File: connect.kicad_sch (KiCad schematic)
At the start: 37 parts, among them J101 Cortex, J102 DX07S016JA3, SW101 SKSG, SW102 SKSG, SW103 SKSG, SW104 SKSG, SW105 SKSG, U101 TPS78433QWDRBRQ1, U102 ATSAMD51J, Y101 32k768

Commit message: Refresh
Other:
- moved on the sheet: D102, D103, ESD101

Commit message: Export stencil
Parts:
- C107, C110: Manufacturer YAGEO -> TDK; Mouser 603-CC603JRNPO9BN180 -> 810-CGA3E2C0G1H180J; Product CC0603JRNPO9BN180 -> CGA3E2C0G1H180J080AA
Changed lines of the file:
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@@
 	(title_block
 		(title "V2 connect")
-		(date "2026-02-12")
+		(date "2026-03-02")
 		(rev "2026-02-12")
 		(company "Versio Duo")
@@
 			)
 		)
-		(property "Mouser" "603-CC603JRNPO9BN180"
+		(property "Mouser" "810-CGA3E2C0G1H180J"
 			(at 0.762 43.18 0)
 			(show_name yes)
@@
 			)
 		)
-		(property "Product" "CC0603JRNPO9BN180"
+		(property "Product" "CGA3E2C0G1H180J080AA"
 			(at 3.556 43.18 0)
 			(show_name yes)
@@
 			)
 		)
-		(property "Manufacturer" "YAGEO"
+		(property "Manufacturer" "TDK"
 			(at 6.35 43.18 0)
 			(show_name yes)
@@
 			)
 		)
-		(property "Mouser" "603-CC603JRNPO9BN180"
+		(property "Mouser" "810-CGA3E2C0G1H180J"
 			(at 0.762 38.1 0)
 			(show_name yes)
@@
 			)
 		)
-		(property "Product" "CC0603JRNPO9BN180"
+		(property "Product" "CGA3E2C0G1H180J080AA"
 			(at 3.556 38.1 0)
 			(show_name yes)
@@
 			)
 		)
-		(property "Manufacturer" "YAGEO"
+		(property "Manufacturer" "TDK"
 			(at 6.35 38.1 0)
 			(show_name yes)

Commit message: Replace diode
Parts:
- D102, D103, D104: Rating (none) -> 60V
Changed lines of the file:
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@@
 	(title_block
 		(title "V2 connect")
-		(date "2026-03-02")
-		(rev "2026-02-12")
+		(date "2026-03-12")
+		(rev "2026-03-12")
 		(company "Versio Duo")
 	)
@@
 			)
 		)
-		(property "Description" "Unpolarized capacitor, small symbol"
+		(property "Description" ""
 			(at 57.15 171.45 0)
 			(effects
@@
 			)
 		)
-		(property "Description" "Push button switch, generic, two pins"
+		(property "Description" "Push button"
 			(at 264.16 24.13 0)
 			(effects
@@
 			)
 		)
-		(property "Description" "Unpolarized capacitor, small symbol"
+		(property "Description" ""
 			(at 88.9 39.37 0)
 			(effects
@@
 			)
 		)
-		(property "Description" "Two pin crystal, small symbol"
+		(property "Description" ""
 			(at 26.67 40.64 0)
 			(effects
@@
 			)
 		)
-		(property "Description" "Light emitting diode, small symbol"
+		(property "Description" ""
 			(at 132.08 58.42 0)
 			(effects
@@
 			)
 		)
-		(property "Description" "Unpolarized capacitor, small symbol"
+		(property "Description" ""
 			(at 198.12 54.61 0)
 			(effects
@@
 			)
 		)
-		(property "Description" "Unpolarized capacitor, small symbol"
+		(property "Description" ""
 			(at 9.652 43.18 0)
 			(effects
@@
 			)
 		)
-		(property "Description" "Resistor, small symbol"
+		(property "Description" ""
 			(at 219.71 88.9 0)
 			(effects
@@
 			)
 		)
-		(property "Description" "Push button switch, generic, two pins"
+		(property "Description" "Push button"
 			(at 264.16 58.42 0)
 			(effects
@@
 			)
 		)
+		(property "Rating" "60V"
+			(at 71.12 137.16 0)
+			(effects
+				(font
+					(size 1.27 1.27)
+				)
+				(hide yes)
+			)
+		)
 		(pin "1"
 		)
@@
 			)
 		)
-		(property "Description" "Unpolarized capacitor, small symbol"
+		(property "Description" ""
 			(at 173.99 54.61 0)
 			(effects
@@
 			)
 		)
-		(property "Description" "Unpolarized capacitor, small symbol"
+		(property "Description" ""
 			(at 119.38 39.37 0)
 			(effects
@@
 			)
 		)
-		(property "Description" "Resistor, small symbol"
+		(property "Description" ""
 			(at 219.71 91.44 0)
 			(effects
@@
 			)
 		)
+		(property "Rating" "60V"
+			(at 257.81 107.95 0)
+			(effects
+				(font
+					(size 1.27 1.27)
+				)
+				(hide yes)
+			)
+		)
 		(pin "1"
 		)
@@
 			)
 		)
-		(property "Description" "Resistor, small symbol"
+		(property "Description" ""
 			(at 63.5 120.65 0)
 			(effects
@@
 			)
 		)
-		(property "Description" "Unpolarized capacitor, small symbol"
+		(property "Description" ""
 			(at 9.652 38.1 0)
 			(effects
@@
 			)
 		)
-		(property "Description" "Resistor, small symbol"
+		(property "Description" ""
 			(at 152.4 58.42 0)
 			(effects
@@
 			)
 		)
-		(property "Description" "Unpolarized capacitor, small symbol"
+		(property "Description" ""
 			(at 99.06 39.37 0)
 			(effects
@@
 			)
 		)
-		(property "Description" "Unpolarized capacitor, small symbol"
+		(property "Description" ""
 			(at 78.74 39.37 0)
 			(effects
@@
 			)
 		)
-		(property "Description" "Push button switch, generic, two pins"
+		(property "Description" "Push button"
 			(at 133.35 76.2 0)
 			(effects
@@
 			)
 		)
-		(property "Description" "Unpolarized capacitor, small symbol"
+		(property "Description" ""
 			(at 109.22 39.37 0)
 			(effects
@@
 			)
 		)
+		(property "Rating" "60V"
+			(at 257.81 92.71 0)
+			(effects
+				(font
+					(size 1.27 1.27)
+				)
+				(hide yes)
+			)
+		)
 		(pin "1"
 		)
@@
 			)
 		)
-		(property "Description" "Push button switch, generic, two pins"
+		(property "Description" "Push button"
 			(at 264.16 46.99 0)
 			(effects
@@
 			)
 		)
-		(property "Description" "Unpolarized capacitor, small symbol"
+		(property "Description" ""
 			(at 57.15 41.91 0)
 			(effects
@@
 			)
 		)
-		(property "Description" "Push button switch, generic, two pins"
+		(property "Description" "Push button"
 			(at 264.16 35.56 0)
 			(effects

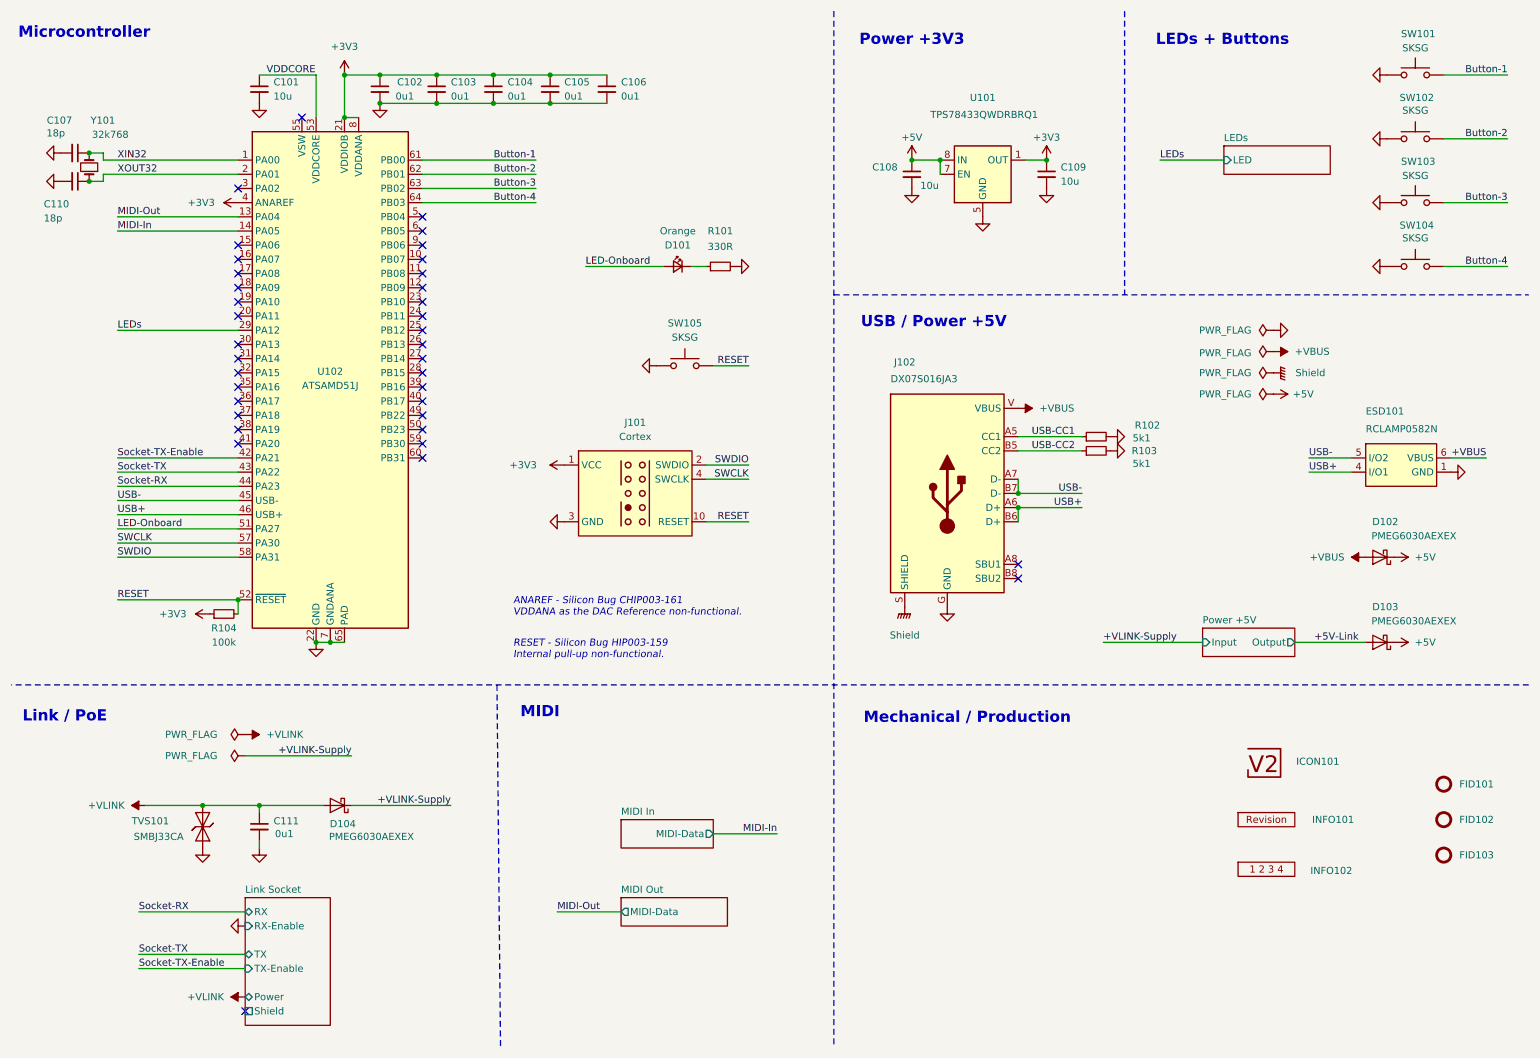
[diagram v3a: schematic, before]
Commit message: Update ESD suppressor
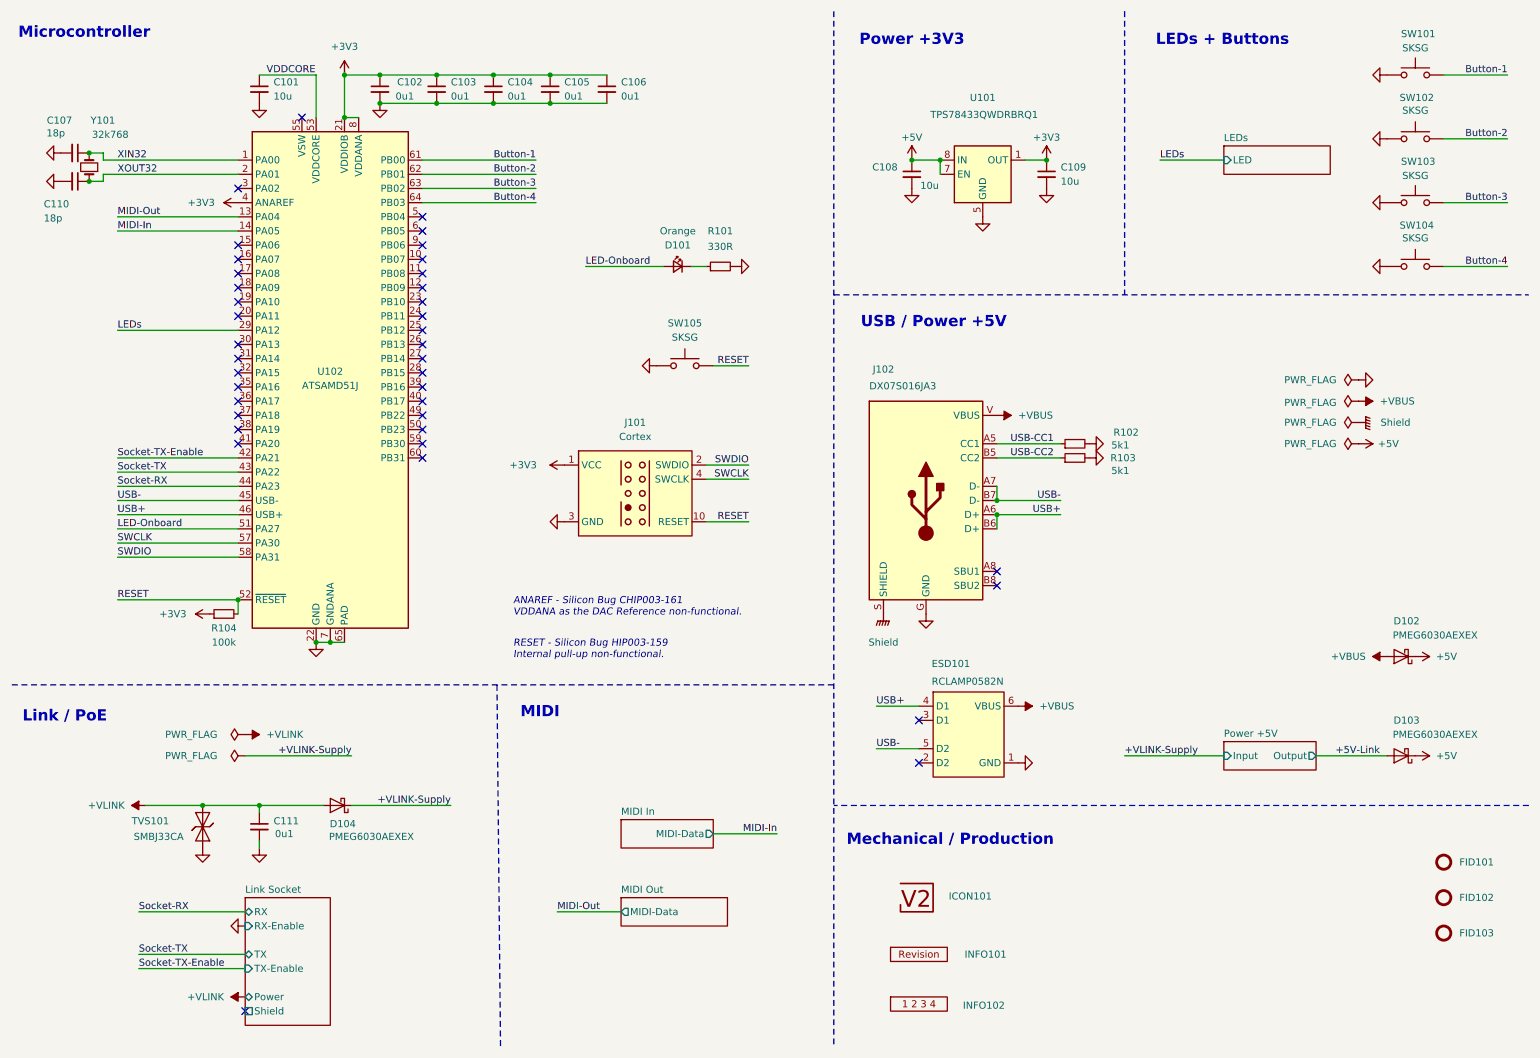
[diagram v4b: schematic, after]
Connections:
- no-connect marks 37 -> 39
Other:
- moved on the sheet: D102, D103, FID101, FID102, FID103, ICON101, INFO101, INFO102, J102, R102, R103

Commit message: Update
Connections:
- net USB+: now also ESD101.3 (D1)
- net USB-: now also ESD101.2 (D2)
- no-connect marks 39 -> 37
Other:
- moved on the sheet: D102, D103
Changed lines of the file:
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@@
 	)
 	(junction
+		(at 175.26 137.16)
+		(diameter 0)
+		(color 0 0 0 0)
+	)
+	(junction
 		(at 46.99 154.94)
 		(diameter 0)
@@
 	)
 	(junction
+		(at 175.26 144.78)
+		(diameter 0)
+		(color 0 0 0 0)
+	)
+	(junction
 		(at 78.74 29.21)
 		(diameter 0)
@@
 	)
 	(no_connect
-		(at 175.26 147.32)
-	)
-	(no_connect
 		(at 64.77 31.75)
 	)
@@
 	)
 	(no_connect
-		(at 175.26 139.7)
-	)
-	(no_connect
 		(at 86.36 72.39)
 	)
@@
 	(wire
 		(pts
-			(xy 246.38 146.05) (xy 259.08 146.05)
+			(xy 247.65 137.16) (xy 260.35 137.16)
 		)
 		(stroke
@@
 	(wire
 		(pts
-			(xy 229.87 146.05) (xy 212.09 146.05)
+			(xy 231.14 137.16) (xy 213.36 137.16)
 		)
 		(stroke
@@
 	(wire
 		(pts
+			(xy 175.26 137.16) (xy 175.26 139.7)
+		)
+		(stroke
+			(width 0)
+			(type default)
+		)
+	)
+	(wire
+		(pts
 			(xy 26.67 43.18) (xy 29.21 43.18)
 		)
@@
 	(wire
 		(pts
+			(xy 175.26 144.78) (xy 175.26 147.32)
+		)
+		(stroke
+			(width 0)
+			(type default)
+		)
+	)
+	(wire
+		(pts
 			(xy 137.16 96.52) (xy 144.78 96.52)
 		)
@@
 	)
 	(label "+5V-Link"
-		(at 257.81 146.05 180)
+		(at 259.08 137.16 180)
 		(effects
 			(font
@@
 	)
 	(label "+VLINK-Supply"
-		(at 212.09 146.05 0)
+		(at 213.36 137.16 0)
 		(effects
 			(font
@@
 	(symbol
 		(lib_id "V2_power:+5V")
-		(at 264.16 146.05 270)
+		(at 265.43 137.16 270)
 		(unit 1)
 		(exclude_from_sim no)
@@
 		(dnp no)
 		(property "Reference" "#PWR130"
-			(at 260.35 146.05 0)
+			(at 261.62 137.16 0)
 			(effects
 				(font
@@
 		)
 		(property "Value" "+5V"
-			(at 269.748 146.05 90)
+			(at 271.018 137.16 90)
 			(effects
 				(font
@@
 		)
 		(property "Footprint" ""
-			(at 264.16 146.05 0)
+			(at 265.43 137.16 0)
 			(effects
 				(font
@@
 		)
 		(property "Datasheet" ""
-			(at 264.16 146.05 0)
+			(at 265.43 137.16 0)
 			(effects
 				(font
@@
 		)
 		(property "Description" ""
-			(at 264.16 146.05 0)
+			(at 265.43 137.16 0)
 			(effects
 				(font
@@
 	(symbol
 		(lib_id "V2_power:+5V")
-		(at 264.16 128.27 270)
+		(at 265.43 119.38 270)
 		(unit 1)
 		(exclude_from_sim no)
@@
 		(dnp no)
 		(property "Reference" "#PWR120"
-			(at 260.35 128.27 0)
+			(at 261.62 119.38 0)
 			(effects
 				(font
@@
 		)
 		(property "Value" "+5V"
-			(at 269.748 128.2699 90)
+			(at 271.018 119.3799 90)
 			(effects
 				(font
@@
 		)
 		(property "Footprint" ""
-			(at 264.16 128.27 0)
+			(at 265.43 119.38 0)
 			(effects
 				(font
@@
 		)
 		(property "Datasheet" ""
-			(at 264.16 128.27 0)
+			(at 265.43 119.38 0)
 			(effects
 				(font
@@
 		)
 		(property "Description" ""
-			(at 264.16 128.27 0)
+			(at 265.43 119.38 0)
 			(effects
 				(font
@@
 	(symbol
 		(lib_id "V2_Diode:PMEG6030AEXEX")
-		(at 261.62 146.05 180)
+		(at 262.89 137.16 180)
 		(unit 1)
 		(exclude_from_sim no)
@@
 		(dnp no)
 		(property "Reference" "D103"
-			(at 264.922 139.7 0)
+			(at 266.192 130.81 0)
 			(effects
 				(font
@@
 		)
 		(property "Value" "PMEG6030AEXEX"
-			(at 267.716 142.24 0)
+			(at 268.986 133.35 0)
 			(effects
 				(font
@@
 		)
 		(property "Footprint" "V2_Diode_SMD:D_SOD-123HP"
-			(at 261.62 137.668 0)
+			(at 262.89 128.778 0)
 			(effects
 				(font
@@
 		)
 		(property "Datasheet" ""
-			(at 261.62 146.05 0)
+			(at 262.89 137.16 0)
 			(effects
 				(font
@@
 		)
 		(property "Description" ""
-			(at 261.62 146.05 0)
+			(at 262.89 137.16 0)
 			(effects
 				(font
@@
 		)
 		(property "Mouser" "771-PMEG6030AEXEX"
-			(at 261.62 134.874 0)
+			(at 262.89 125.984 0)
 			(effects
 				(font
@@
 		)
 		(property "Manufacturer" "Nexperia"
-			(at 261.62 135.89 0)
+			(at 262.89 127 0)
 			(effects
 				(font
@@
 		)
 		(property "Product" "PMEG6030AEXEX"
-			(at 261.62 133.35 0)
+			(at 262.89 124.46 0)
 			(effects
 				(font
@@
 		)
 		(property "Rating" "60V"
-			(at 261.62 128.27 0)
+			(at 262.89 119.38 0)
 			(effects
 				(font
@@
 	(symbol
 		(lib_id "V2_power:+VBUS")
-		(at 259.08 128.27 90)
+		(at 260.35 119.38 90)
 		(unit 1)
 		(exclude_from_sim no)
@@
 		(fields_autoplaced yes)
 		(property "Reference" "#PWR140"
-			(at 271.78 128.27 0)
+			(at 273.05 119.38 0)
 			(effects
 				(font
@@
 		)
 		(property "Value" "+VBUS"
-			(at 255.27 128.2699 90)
+			(at 256.54 119.3799 90)
 			(effects
 				(font
@@
 		)
 		(property "Footprint" ""
-			(at 259.08 128.27 0)
+			(at 260.35 119.38 0)
 			(effects
 				(font
@@
 		)
 		(property "Datasheet" ""
-			(at 259.08 128.27 0)
+			(at 260.35 119.38 0)
 			(effects
 				(font
@@
 		)
 		(property "Description" "USB Power Delivery"
-			(at 274.574 128.27 0)
+			(at 275.844 119.38 0)
 			(effects
 				(font
@@
 	(symbol
 		(lib_id "V2_Diode:PMEG6030AEXEX")
-		(at 261.62 128.27 180)
+		(at 262.89 119.38 180)
 		(unit 1)
 		(exclude_from_sim no)
@@
 		(dnp no)
 		(property "Reference" "D102"
-			(at 264.922 121.92 0)
+			(at 266.192 113.03 0)
 			(effects
 				(font
@@
 		)
 		(property "Value" "PMEG6030AEXEX"
-			(at 267.716 124.46 0)
+			(at 268.986 115.57 0)
 			(effects
 				(font
@@
 		)
 		(property "Footprint" "V2_Diode_SMD:D_SOD-123HP"
-			(at 261.62 119.888 0)
+			(at 262.89 110.998 0)
 			(effects
 				(font
@@
 		)
 		(property "Datasheet" ""
-			(at 261.62 128.27 0)
+			(at 262.89 119.38 0)
 			(effects
 				(font
@@
 		)
 		(property "Description" ""
-			(at 261.62 128.27 0)
+			(at 262.89 119.38 0)
 			(effects
 				(font
@@
 		)
 		(property "Mouser" "771-PMEG6030AEXEX"
-			(at 261.62 117.094 0)
+			(at 262.89 108.204 0)
 			(effects
 				(font
@@
 		)
 		(property "Manufacturer" "Nexperia"
-			(at 261.62 118.11 0)
+			(at 262.89 109.22 0)
 			(effects
 				(font
@@
 		)
 		(property "Product" "PMEG6030AEXEX"
-			(at 261.62 115.57 0)
+			(at 262.89 106.68 0)
 			(effects
 				(font
@@
 		)
 		(property "Rating" "60V"
-			(at 261.62 110.49 0)
+			(at 262.89 101.6 0)
 			(effects
 				(font
@@
 	)
 	(sheet
-		(at 229.87 143.51)
+		(at 231.14 134.62)
 		(size 16.51 5.08)
 		(exclude_from_sim no)
@@
 		)
 		(property "Sheetname" "Power +5V"
-			(at 229.87 142.7984 0)
+			(at 231.14 133.9084 0)
 			(effects
 				(font
@@
 		)
 		(property "Sheetfile" "PowerSupply.kicad_sch"
-			(at 229.87 149.1746 0)
+			(at 231.14 140.2846 0)
 			(effects
 				(font
@@
 		)
 		(pin "Input" input
-			(at 229.87 146.05 180)
+			(at 231.14 137.16 180)
 			(effects
 				(font
@@
 		)
 		(pin "Output" output
-			(at 246.38 146.05 0)
+			(at 247.65 137.16 0)
 			(effects
 				(font

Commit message: KiCad 10
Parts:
- INFO101: value ~ -> (none)

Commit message: Refresh
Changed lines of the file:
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@@
 	(title_block
 		(title "V2 connect")
-		(date "2026-03-20")
+		(date "2026-03-24")
 		(rev "2026-03-14")
 		(company "Versio Duo")
@@
 	(wire
 		(pts
-			(xy 54.61 146.05) (xy 73.66 146.05)
+			(xy 54.61 146.05) (xy 74.93 146.05)
 		)
 		(stroke
@@
 	)
 	(label "+VLINK-Supply"
-		(at 73.66 146.05 180)
+		(at 74.93 146.05 180)
 		(effects
 			(font
@@
 		(unit 1)
 		(body_style 1)
-		(exclude_from_sim no)
-		(in_bom yes)
-		(on_board yes)
+		(exclude_from_sim yes)
+		(in_bom no)
+		(on_board no)
 		(in_pos_files yes)
 		(dnp no)
@@
 		)
 		(property "Value" "Shield"
-			(at 260.604 86.36 90)
+			(at 261.62 86.36 90)
 			(show_name no)
 			(do_not_autoplace no)
@@
 		(unit 1)
 		(body_style 1)
-		(exclude_from_sim no)
-		(in_bom yes)
-		(on_board yes)
+		(exclude_from_sim yes)
+		(in_bom no)
+		(on_board no)
 		(in_pos_files yes)
 		(dnp no)
-		(fields_autoplaced yes)
 		(property "Reference" "#PWR132"
 			(at 41.91 142.24 0)
@@
 		)
 		(property "Value" "+VLINK"
-			(at 58.42 142.2399 90)
+			(at 59.944 142.2399 90)
 			(show_name no)
 			(do_not_autoplace no)
@@
 		(unit 1)
 		(body_style 1)
-		(exclude_from_sim no)
-		(in_bom yes)
-		(on_board yes)
+		(exclude_from_sim yes)
+		(in_bom no)
+		(on_board no)
 		(in_pos_files yes)
 		(dnp no)
@@
 		(unit 1)
 		(body_style 1)
-		(exclude_from_sim no)
-		(in_bom yes)
-		(on_board yes)
+		(exclude_from_sim yes)
+		(in_bom no)
+		(on_board no)
 		(in_pos_files yes)
 		(dnp no)
@@
 		(unit 1)
 		(body_style 1)
-		(exclude_from_sim no)
-		(in_bom yes)
-		(on_board yes)
+		(exclude_from_sim yes)
+		(in_bom no)
+		(on_board no)
 		(in_pos_files yes)
 		(dnp no)
-		(fields_autoplaced yes)
 		(property "Reference" "#PWR141"
 			(at 180.34 137.16 0)
@@
 		)
 		(property "Value" "+VBUS"
-			(at 196.85 137.1599 90)
+			(at 198.12 137.1599 90)
 			(show_name no)
 			(do_not_autoplace no)
@@
 		(unit 1)
 		(body_style 1)
-		(exclude_from_sim no)
-		(in_bom yes)
-		(on_board yes)
+		(exclude_from_sim yes)
+		(in_bom no)
+		(on_board no)
 		(in_pos_files yes)
 		(dnp no)
@@
 		(unit 1)
 		(body_style 1)
-		(exclude_from_sim no)
-		(in_bom yes)
-		(on_board yes)
+		(exclude_from_sim yes)
+		(in_bom no)
+		(on_board no)
 		(in_pos_files yes)
 		(dnp no)
@@
 		(unit 1)
 		(body_style 1)
-		(exclude_from_sim no)
-		(in_bom yes)
-		(on_board yes)
+		(exclude_from_sim yes)
+		(in_bom no)
+		(on_board no)
 		(in_pos_files yes)
 		(dnp no)
-		(fields_autoplaced yes)
 		(property "Reference" "#PWR138"
 			(at 241.3 82.55 0)
@@
 		)
 		(property "Value" "+VBUS"
-			(at 257.81 82.5499 90)
+			(at 258.572 82.5499 90)
 			(show_name no)
 			(do_not_autoplace no)
@@
 		(unit 1)
 		(body_style 1)
-		(exclude_from_sim no)
-		(in_bom yes)
-		(on_board yes)
+		(exclude_from_sim yes)
+		(in_bom no)
+		(on_board no)
 		(in_pos_files yes)
 		(dnp no)
-		(fields_autoplaced yes)
 		(property "Reference" "#PWR139"
 			(at 176.53 85.09 0)
@@
 		)
 		(property "Value" "+VBUS"
-			(at 193.04 85.0899 90)
+			(at 194.31 85.0899 90)
 			(show_name no)
 			(do_not_autoplace no)

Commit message: Refresh
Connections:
- net VDDCORE renamed +VDDCORE
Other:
- moved on the sheet: C111, D102, D103, D104, ESD101, TVS101
